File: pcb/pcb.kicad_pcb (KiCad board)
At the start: 2 copper layers, 163.6 x 116.9 mm, 91 parts, among them J1 USB-Mini, J2 Conn_01x05, P1 i2c-pin1, P2 i2c-pin2, SW1 SW_Push, SW10 SW_Push, SW11 SW_Push, SW12 SW_Push, SW13 SW_Push, SW14 SW_Push, SW15 SW_Push, SW16 SW_Push, SW17 SW_Push, SW18 SW_Push, SW19 SW_Push, SW2 SW_Push, SW20 SW_Push, SW21 SW_Push, SW22 SW_Push, SW23 SW_Push, SW24 SW_Push, SW25 SW_Push, SW26 SW_Push, SW27 SW_Push, SW28 SW_Push, SW29 SW_Push, SW3 SW_Push, SW30 SW_Push, SW31 SW_Push, SW32 SW_Push, SW33 SW_Push, SW34 SW_Push, SW35 SW_Push, SW36 SW_Push, SW37 SW_Push, SW38 SW_Push, SW39 SW_Push, SW4 SW_Push, SW40 SW_Push, SW41 SW_Push, SW42 Rotary_Encoder_Switch, SW5 SW_Push, SW6 SW_Push, SW7 SW_Push, SW8 SW_Push, SW9 SW_Push, U1 ProMicro, U2 TRRS

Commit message: added missing via…
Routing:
- net GND: vias 5 -> 6

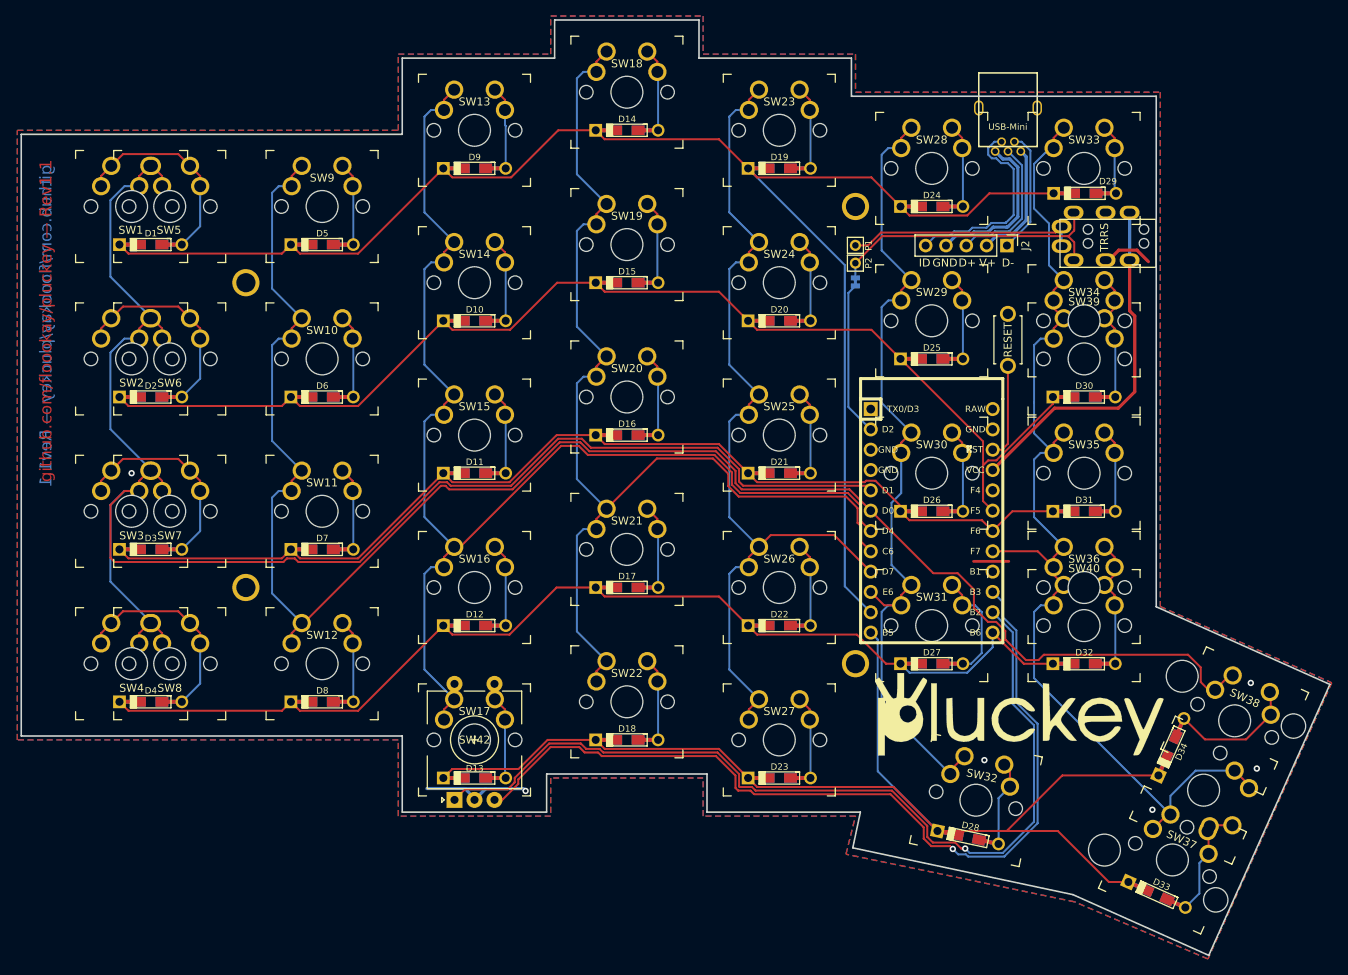
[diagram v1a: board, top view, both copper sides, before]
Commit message: added a key and moved a inner key for 5x7
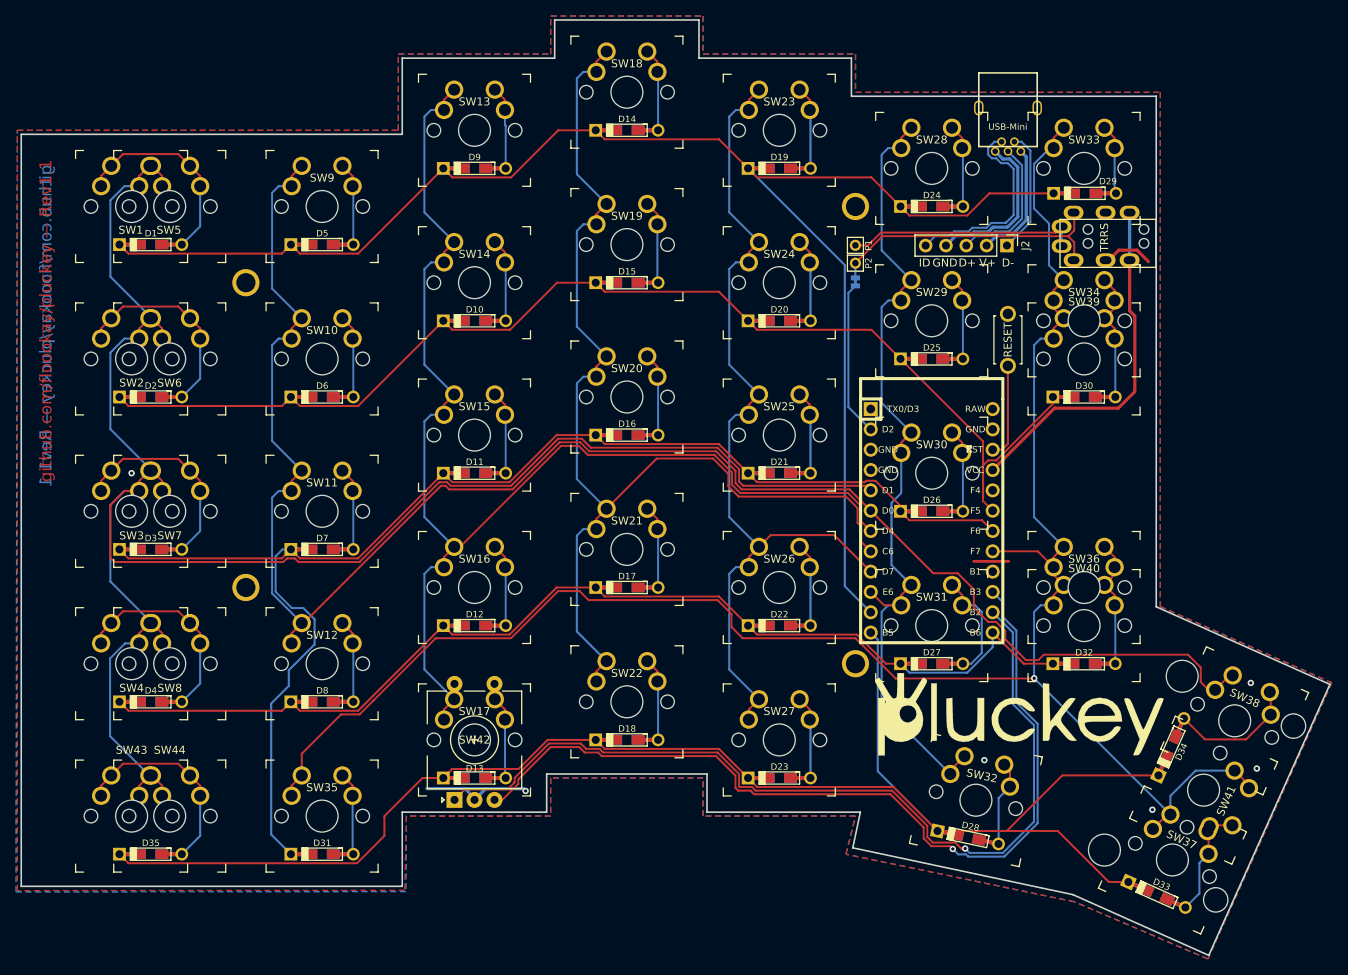
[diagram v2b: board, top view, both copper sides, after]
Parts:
- added D35: D, Keebio-Parts:Diode-dual, F.Cu at (40.5, 164.3)
- added SW43: SW_Push, keyswitches:SW_MX_reversible, F.Cu at (38.1, 159.5)
- added SW44: SW_Push, keyswitches:SW_MX_reversible, F.Cu at (42.9, 159.5)
- moved D31 104.4 mm to (61.9, 164.3)
- moved SW35 104.4 mm to (61.9, 159.5)
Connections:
- U1 pad 1: Net-(U1-Pad1) -> unconnected-(U1-Pad1)
- U1 pad 16: Net-(U1-Pad16) -> unconnected-(U1-Pad16)
- U1 pad 20: Net-(U1-Pad20) -> unconnected-(U1-Pad20)
- U1 pad 24: Net-(U1-Pad24) -> unconnected-(U1-Pad24)
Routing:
- net /col6: track 137.2 -> 274.8 mm, vias 0 -> 1
- net /row4: track 147.3 -> 194.1 mm
- net /row2: track 132.2 -> 169.0 mm
- net /col0: track 205.1 -> 232.3 mm
- net Net-(D35-Pad2): track 0.00 -> 25.4 mm
- net Net-(JP1-Pad2): track 36.7 -> 56.2 mm
- net /data: track 19.4 -> 0.00 mm
- net Net-(D32-Pad2): track 16.2 -> 0.00 mm
- net Net-(D30-Pad2): track 16.2 -> 0.00 mm
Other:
- outline, holes or cut-outs redrawn
- net class Default removed
- net class GND removed
- net class VCC removed
- net class thick_header removed
